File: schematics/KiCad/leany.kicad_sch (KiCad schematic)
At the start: 34 parts, among them J1 SWD, J2 SSD1306, J3 USB_C, Q1 DMG6601LVT-7, SW2 ZERO_BTN, SW3 HOLD_BTN, U1 STM32F103C8Tx, U2 AP2112K-3.3, U3 LSM6DSO, U4 CH340C, Y1 8MHz

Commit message: add RGB status led
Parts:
- added D2: ASMB-MTB1-0B3A2, LED_SMD:LED_Avago_PLCC4_3.2x2.8mm_CW, symbol LED:ASMB-MTB1-0A3A2
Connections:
- no-connect marks 23 -> 27
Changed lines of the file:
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@@
+	)
+	(no_connect
+		(at 40.64 111.76)
+	)
+	(no_connect
+		(at 30.48 111.76)
 	)
 	(no_connect
@@
 	)
 	(no_connect
+		(at 30.48 116.84)
+	)
+	(no_connect
 		(at 86.36 166.37)
 	)
@@
 	(no_connect
 		(at 200.66 58.42)
+	)
+	(no_connect
+		(at 30.48 106.68)
 	)
 	(no_connect
@@
 					(unit 1)
 				)
+			)
+		)
+	)
+	(symbol
+		(lib_id "LED:ASMB-MTB1-0A3A2")
+		(at 35.56 111.76 0)
+		(unit 1)
+		(exclude_from_sim no)
+		(in_bom yes)
+		(on_board yes)
+		(dnp no)
+		(fields_autoplaced yes)
+		(property "Reference" "D2"
+			(at 35.56 96.52 0)
+			(effects
+				(font
+					(size 1.27 1.27)
+				)
+			)
+		)
+		(property "Value" "ASMB-MTB1-0B3A2"
+			(at 35.56 99.06 0)
+			(effects
+				(font
+					(size 1.27 1.27)
+				)
+			)
+		)
+		(property "Footprint" "LED_SMD:LED_Avago_PLCC4_3.2x2.8mm_CW"
+			(at 35.56 96.52 0)
+			(effects
+				(font
+					(size 1.27 1.27)
+				)
+				(hide yes)
+			)
+		)
+		(property "Datasheet" "https://docs.broadcom.com/doc/ASMB-MTB1-0B3A2-PLCC-4-Tricolor-Black-Surface-LED-DS"
+			(at 35.56 123.19 0)
+			(effects
+				(font
+					(size 1.27 1.27)
+				)
+				(hide yes)
+			)
+		)
+		(property "Description" "Tricolor Black Surface LED, Common Anode Pin 4, PLCC-4"
+			(at 35.56 111.76 0)
+			(effects
+				(font
+					(size 1.27 1.27)
+				)
+				(hide yes)
+			)
+		)
+		(pin "2"
+		)
+		(pin "1"
+		)
+		(pin "4"
+		)
+		(pin "3"
+		)
+		(instances
+			(project ""
+				(path "/e47b2519-93ca-4a48-9414-ecc253dd35f5"
+					(reference "D2")
+					(unit 1)
+				)

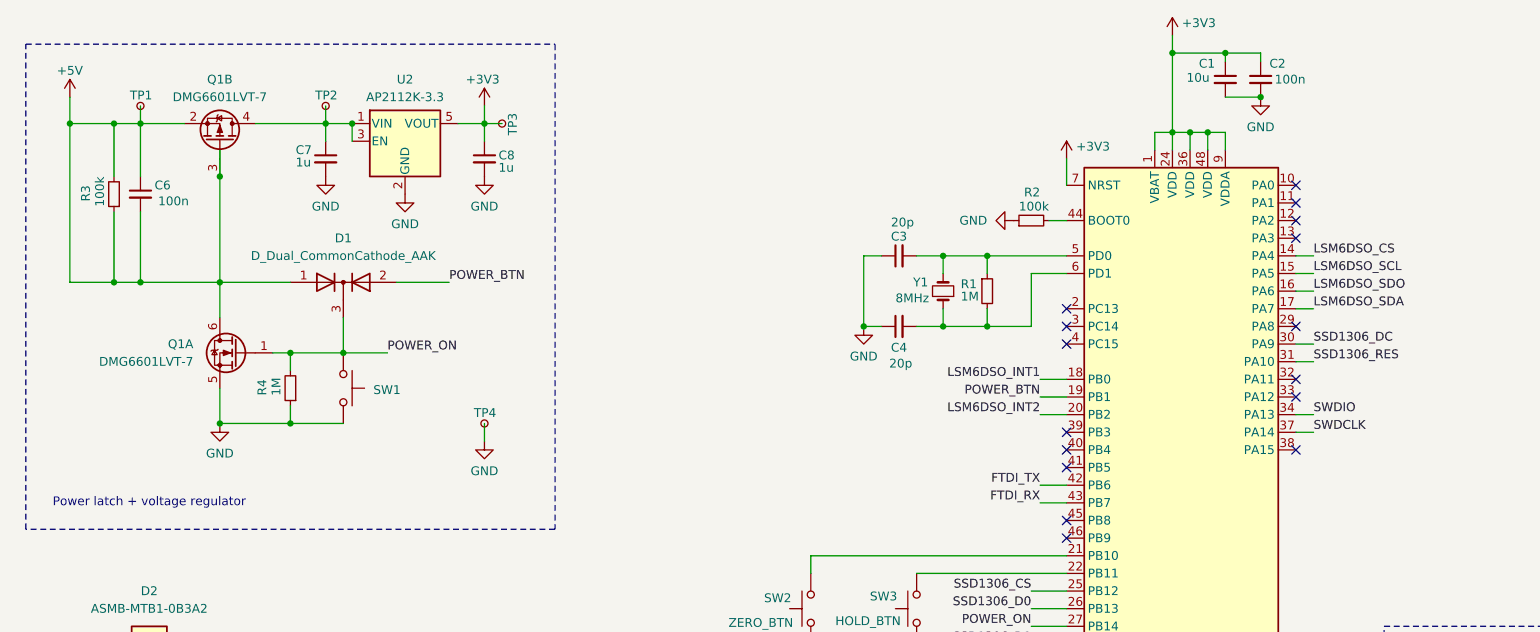
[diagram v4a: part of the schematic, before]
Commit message: move FTDI to pins PA9 and PA10
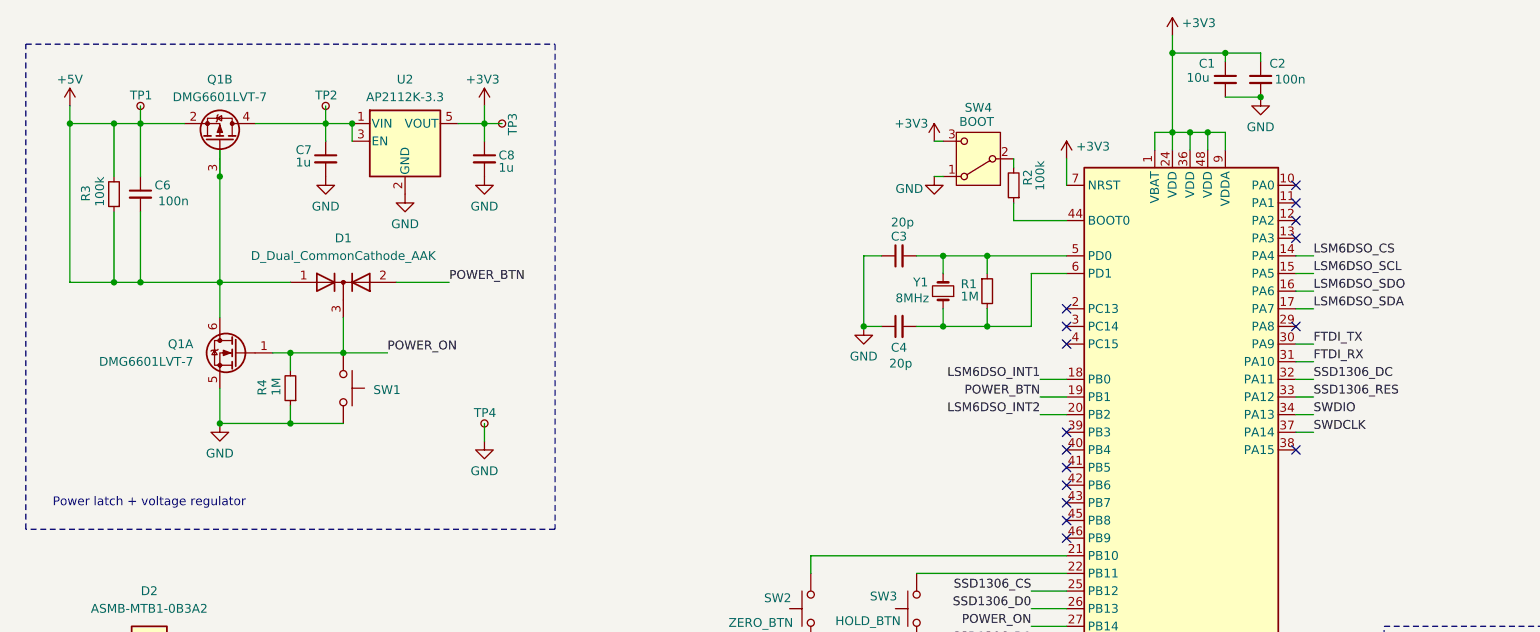
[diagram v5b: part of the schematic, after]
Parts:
- added SW4: BOOT, symbol Switch:SW_SPDT
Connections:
- net +3V3: now also SW4.3 (C)
- net FTDI_RX: now also U1.31 (PA10); no longer U1.43 (PB7)
- net FTDI_TX: now also U1.30 (PA9); no longer U1.42 (PB6)
- net GND: now also SW4.1 (A); no longer R2.1
- net SSD1306_DC: now also U1.32 (PA11); no longer U1.30 (PA9)
- net SSD1306_RES: now also U1.33 (PA12); no longer U1.31 (PA10)
- net at U1.44 (BOOT0): now also R2.1; no longer R2.2
- new net: R2.2, SW4.2 (B)
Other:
- moved on the sheet: R2

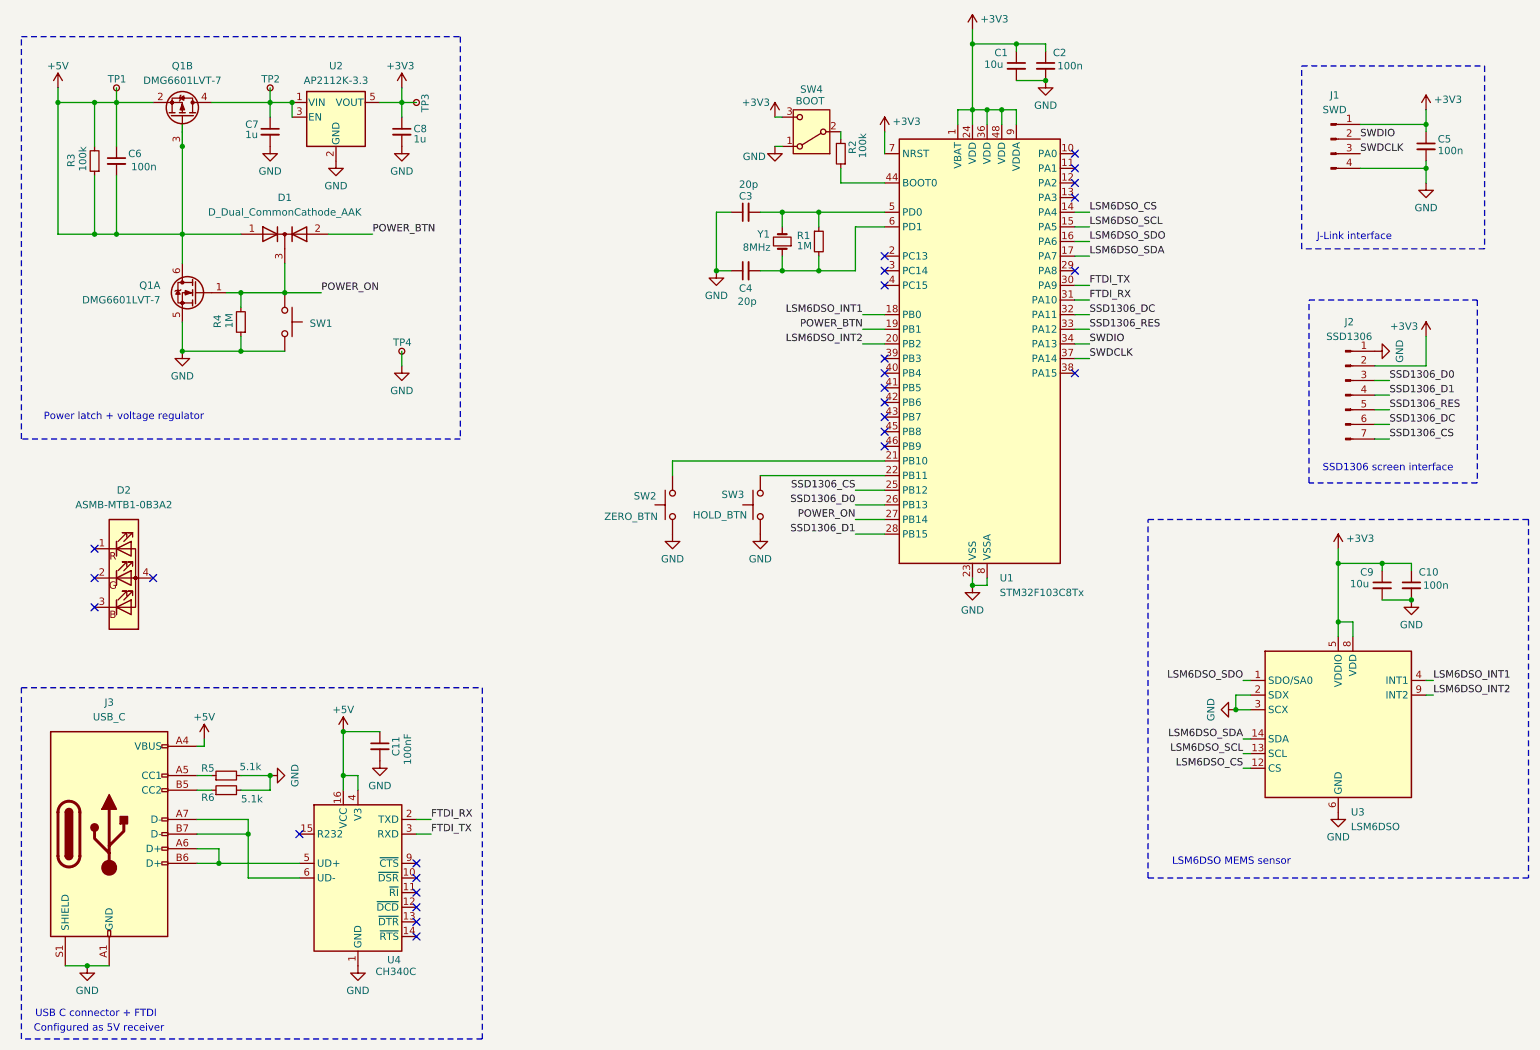
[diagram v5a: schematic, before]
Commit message: add the FTDI reset signal
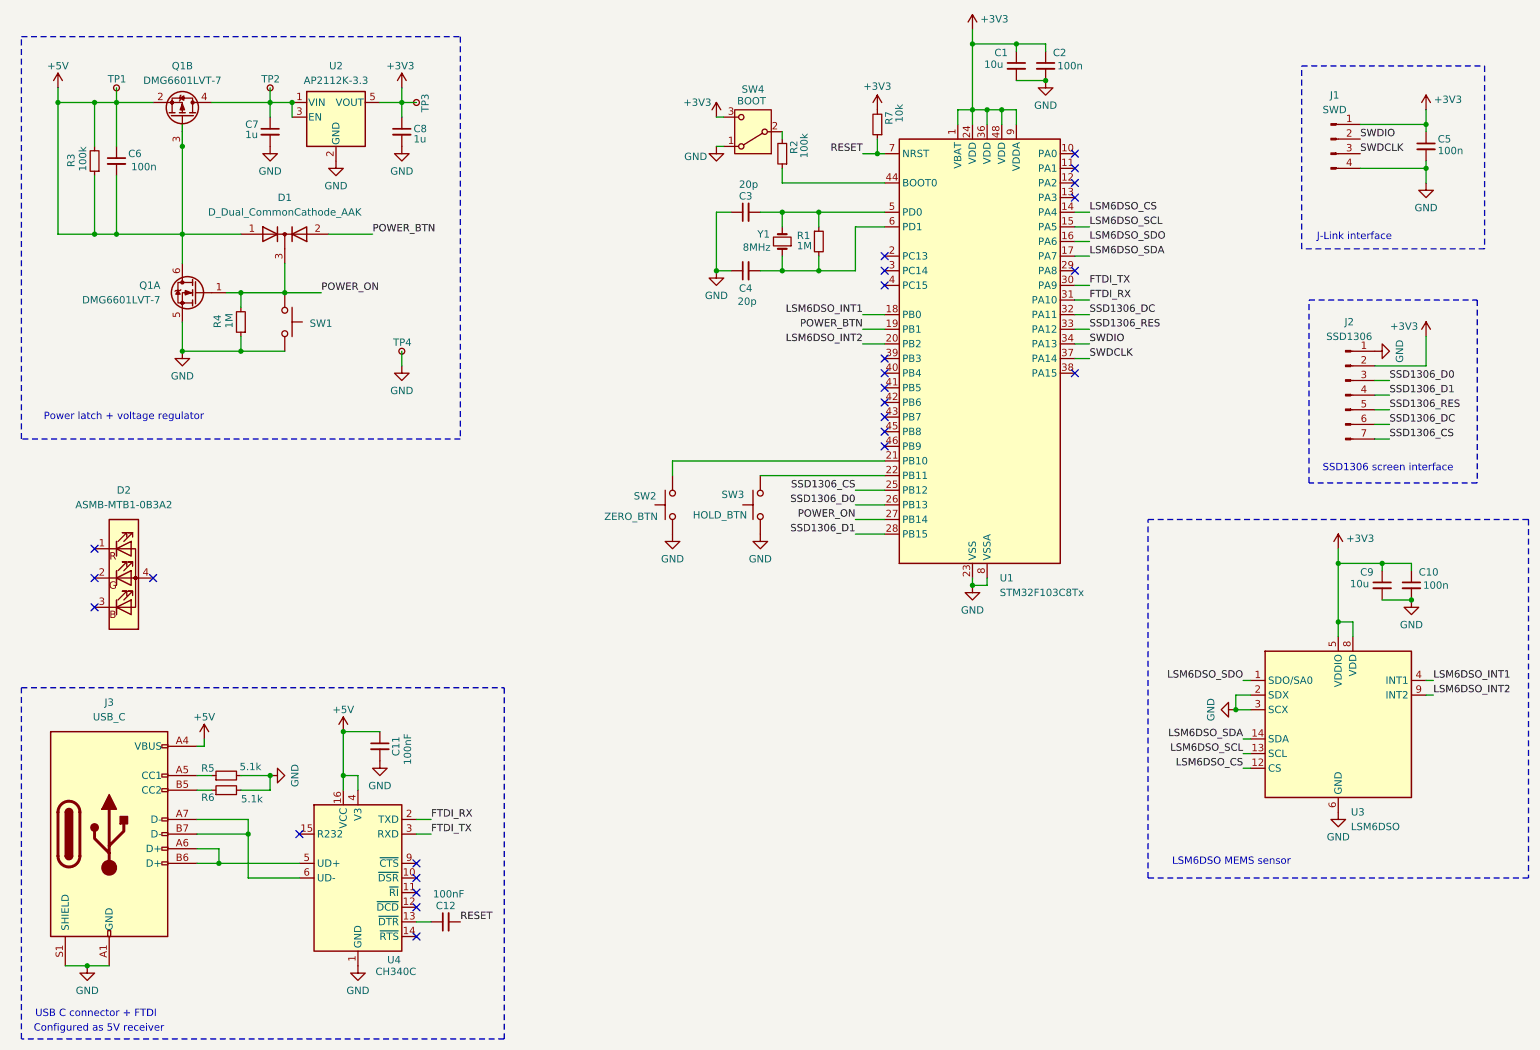
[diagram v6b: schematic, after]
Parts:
- added C12: 100nF, Capacitor_SMD:C_0201_0603Metric, symbol Device:C_Small
- added R7: 10k, Resistor_SMD:R_0603_1608Metric, symbol Device:R_Small
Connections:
- net +3V3: now also R7.2; no longer U1.7 (NRST)
- net at U4.13 (~{DTR}): now also C12.1
- new net RESET: C12.2, R7.1, U1.7 (NRST)
- no-connect marks 27 -> 26
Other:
- moved on the sheet: R2, SW4

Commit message: improve schematics
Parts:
- removed C1, C9: 10u, Capacitor_SMD:C_0201_0603Metric, symbol Device:C_Small
- removed C11, C12: 100nF, Capacitor_SMD:C_0201_0603Metric, symbol Device:C_Small
- removed C2: 100n, Capacitor_SMD:C_0201_0603Metric, symbol Device:C_Small
- removed C7, C8: 1u, Capacitor_SMD:C_0201_0603Metric, symbol Device:C_Small
- removed D1: D_Dual_CommonCathode_AAK, symbol Device:D_Dual_CommonCathode_AAK
- removed J3: USB_C, Connector_USB:USB_C_Receptacle_GCT_USB4105-xx-A_16P_TopMnt_Horizontal, symbol Connector:USB_C_Receptacle_USB2.0_14P
- removed Q1: DMG6601LVT-7, Package_TO_SOT_SMD:TSOT-23-6, symbol leany-symbols:DMG6601LVT-7
- removed R6: 5.1k, Resistor_SMD:R_0603_1608Metric, symbol Device:R_Small
- removed R7: 10k, Resistor_SMD:R_0603_1608Metric, symbol Device:R_Small
- removed SW1: ~, symbol Switch:SW_Push
- removed TP1: 5V, TestPoint:TestPoint_Pad_1.0x1.0mm, symbol Connector:TestPoint_Small
- removed TP2: Vin, TestPoint:TestPoint_Pad_1.0x1.0mm, symbol Connector:TestPoint_Small
- removed TP3: 3.3V, TestPoint:TestPoint_Pad_1.0x1.0mm, symbol Connector:TestPoint_Small
- removed TP4: GND, TestPoint:TestPoint_Pad_1.0x1.0mm, symbol Connector:TestPoint_Small
- removed U2: AP2112K-3.3, Package_TO_SOT_SMD:SOT-23-5, symbol Regulator_Linear:AP2112K-3.3
- removed U4: CH340C, Package_SO:SOIC-16_3.9x9.9mm_P1.27mm, symbol Interface_USB:CH340C
- added C1: 10u, symbol Device:C_Polarized_Small
- added C10: 100nF, Capacitor_SMD:C_0201_0603Metric, symbol Device:C_Small
- added C3, C4, C5: 100n, Capacitor_SMD:C_0201_0603Metric, symbol Device:C_Small
- added U3: CH340C, Package_SO:SOIC-16_3.9x9.9mm_P1.27mm, symbol Interface_USB:CH340C
- R3: value 100k -> 820R
- R4: value 1M -> 820R
- R5: value 5.1k -> 820R
- SW1: renamed from SW4; value BOOT -> BOOTMODE_SW
- renumbered C10 to C2, C5 to C7, C3 to C8, C4 to C9, D2 to D1, U3 to U1, U1 to U2
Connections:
- net RESET is gone; now on net +3V3: U2.7 (NRST)
- net +3V3: now also C6.1, D1.4 (A), C1.1, C10.1, C3.1, C4.1, C5.1, U3.16 (VCC), U3.4 (V3)
- net GND: now also C6.2, SW3.1, C1.2, C10.2, C3.2, C4.2, C5.2, U3.1 (GND); no longer R4.1, R5.2, SW3.2
- net POWER_ON: no longer R4.2
- net at D1.1 (RK): now also R3.1
- net at D1.2 (GK): now also R4.1
- net at D1.3 (BK): now also R5.1
- net LED_RED: now reaches U2.10 (PA0)
- net LED_RED: now also R3.2
- net LED_GREEN: now reaches U2.11 (PA1)
- net LED_GREEN: now also R4.2
- net LED_BLUE: now reaches U2.12 (PA2)
- net LED_BLUE: now also R5.2
- net BATT_VOLT: now reaches U2.13 (PA3)
- net at U2.22 (PB11): now also SW3.2; no longer SW3.1
- net BATT_EN: now reaches U2.29 (PA8)
- net BAT_ACOK: now reaches U2.3 (PC14)
- net BAT_CHGOK: now reaches U2.4 (PC15)
- net BOOT0: now reaches R2.1, U2.44 (BOOT0)
- removed net +5V: C6.1, C6.2, R3.1, R3.2
- net FTDI_RX renamed USART1_RX
- net USART1_RX: now also U3.2 (TXD)
- net FTDI_TX renamed USART1_TX
- net USART1_TX: now also U3.3 (RXD)
- new net USB_D+: U3.5 (UD+)
- new net USB_D-: U3.6 (UD-)
- no-connect marks 26 -> 16
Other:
- added sheet Power management (power_management.kicad_sch)
- note added: "FTDI UART to USB + boot mode switch for programming"
- note added: "RGB status LED"
- note removed: "Configured as 5V receiver"
- note removed: "Power latch + voltage regulator"
- note removed: "USB C connector + FTDI"
- moved on the sheet: C2, C7, C8, C9, D1, J1, J2, R1, R2, SW1, SW2, SW3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
